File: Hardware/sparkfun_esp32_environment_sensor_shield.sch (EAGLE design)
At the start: 53 parts, among them J1 WEATHER_METER-WIND, J2 WEATHER_METER-RAIN, U1 BME280, U2 CCS811, U3 APDS-9301, U4 TVS Diode

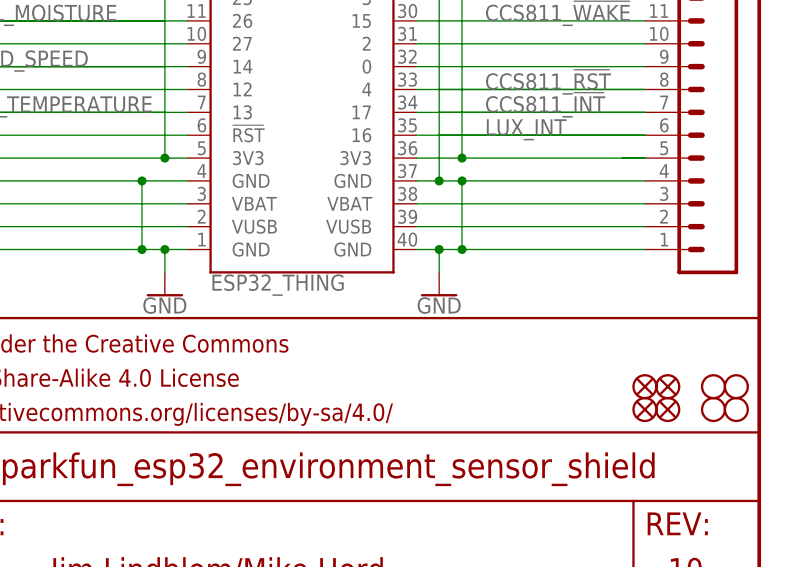
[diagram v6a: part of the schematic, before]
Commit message: Removed restrict layers on antenna for panelization
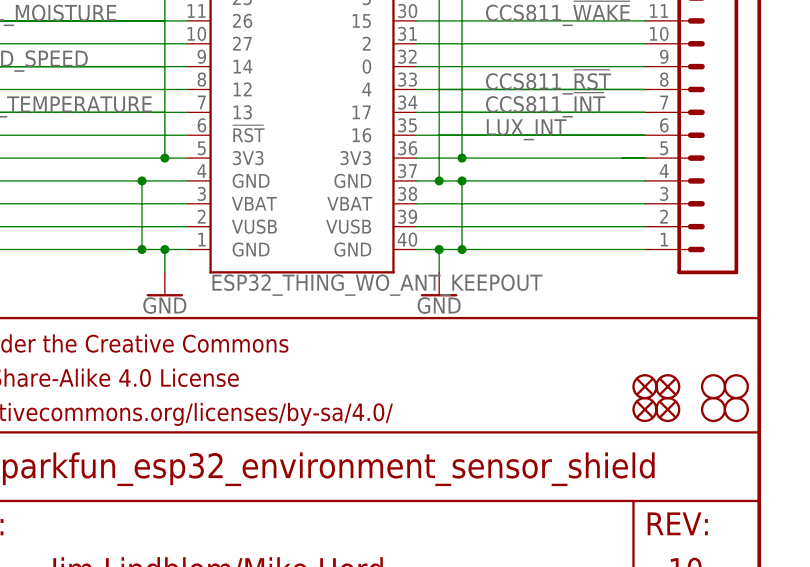
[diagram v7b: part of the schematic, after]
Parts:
- B1: value ESP32_THING -> ESP32_THING_WO_ANT_KEEPOUT; device SparkFun-Boards:ESP32_THING -> SparkFun-Boards:ESP32_THING_WO_ANT_KEEPOUT
- R12: PROD_ID N/A -> (none)
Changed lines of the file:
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@@
 <parts>
 <part name="FRAME1" library="SparkFun-Aesthetics" deviceset="FRAME-LETTER" device=""/>
-<part name="B1" library="SparkFun-Boards" deviceset="ESP32_THING" device=""/>
+<part name="B1" library="SparkFun-Boards" deviceset="ESP32_THING" device="_WO_ANT_KEEPOUT"/>
 <part name="GND17" library="SparkFun-PowerSymbols" deviceset="GND" device=""/>
 <part name="GND19" library="SparkFun-PowerSymbols" deviceset="GND" device=""/>
@@
 <part name="JP5" library="SparkFun-Jumpers" deviceset="JUMPER-SMT_3_2-NC_TRACE" device="_SILK" value=""/>
 <part name="R8" library="esp32-environ-monitor-temp" deviceset="NTC-THERMISTOR" device="-0603" value="10k"/>
-<part name="R12" library="esp32-environ-monitor-temp" deviceset="NTC-THERMISTOR" device="-AXIAL-0.1" value="DNP">
-<attribute name="PROD_ID" value="N/A"/>
-</part>
+<part name="R12" library="esp32-environ-monitor-temp" deviceset="NTC-THERMISTOR" device="-AXIAL-0.1" value="DNP"/>
 <part name="LOGO1" library="SparkFun-Aesthetics" deviceset="SFE_LOGO_NAME" device=".1_INCH"/>
 <part name="LOGO4" library="SparkFun-Aesthetics" deviceset="OSHW-LOGO" device="S"/>
